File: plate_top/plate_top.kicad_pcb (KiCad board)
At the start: 2 copper layers, 157.5 x 118.1 mm, 31 parts, among them SW1 SW_Push

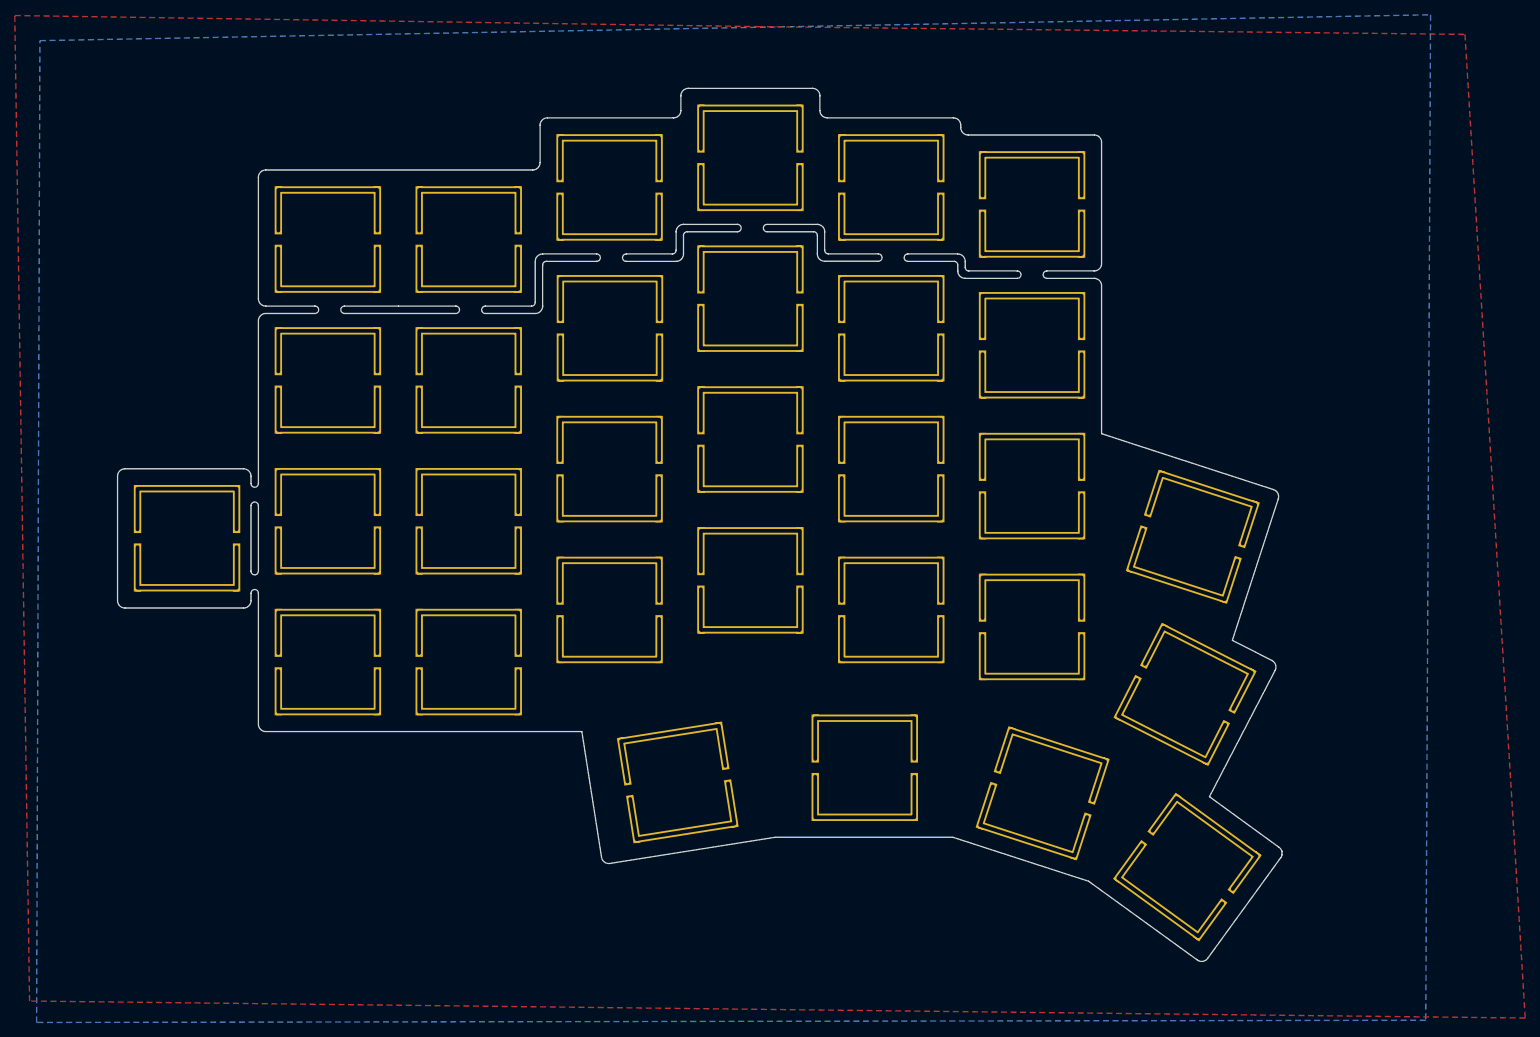
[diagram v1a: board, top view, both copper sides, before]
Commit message: Working on a new design for the top plate.
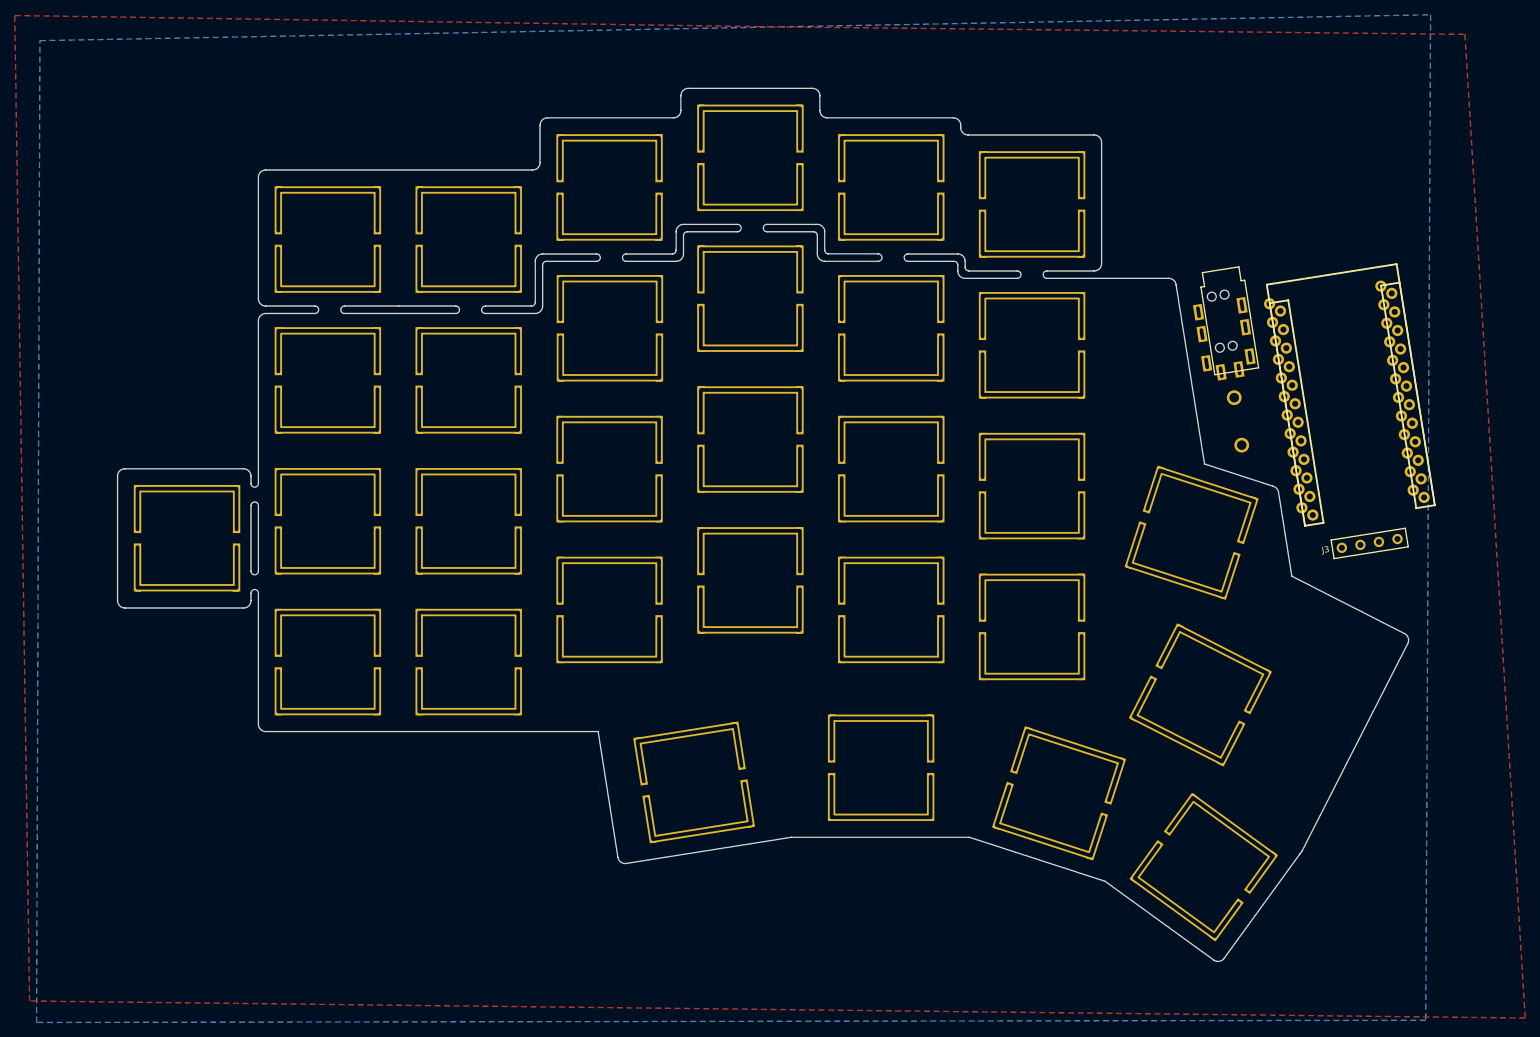
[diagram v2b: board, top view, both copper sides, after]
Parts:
- removed the SW1 at (221.3, 135.9)
- removed the SW1 at (201.7, 125.9)
- removed the SW1 at (177.6, 122.5)
- removed the SW1 at (152.3, 124.4)
- removed the SW1 at (220.9, 112.5)
- removed the SW1 at (222.0, 91.2)
- added J1: TRRS, used_footprints:MJ-4PP-9, F.Cu at (226.1, 57.0)
- added J3: OLED, used_footprints:OLED_4Pin, F.Cu at (242.2, 92.7)
- added SW20: SW_Push, used_footprints:metallized_breakout_cutout, F.Cu at (221.8, 90.7)
- added SW27: SW_Push, used_footprints:metallized_breakout_cutout, F.Cu at (223.0, 112.6)
- added SW28: SW_Push, used_footprints:metallized_breakout_cutout, F.Cu at (154.5, 124.4)
- added SW29: SW_Push, used_footprints:metallized_breakout_cutout, F.Cu at (179.8, 122.5)
- added SW30: SW_Push, used_footprints:metallized_breakout_cutout, F.Cu at (203.9, 125.9)
- added SW31: SW_Push, used_footprints:metallized_breakout_cutout, F.Cu at (223.5, 135.9)
- added SW32: SW_Push, used_footprints:Switch_Reset_THT, F.Cu at (228.1, 75.6)
- added U1: ProMicro, used_footprints:ProMicro_rev2, F.Cu at (243.4, 72.9)
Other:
- board size 157.5 x 118.1 mm -> 174.6 x 118.1 mm

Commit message: Multiple fixes...
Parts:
- moved SW32 32.4 mm to (251.4, 98.1), turned to 81 degrees

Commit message: top + bottom plates
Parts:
- removed J1: TRRS, used_footprints:MJ-4PP-9
- removed J3: OLED, used_footprints:OLED_4Pin
- removed the SW1 at (105.0, 89.1)
- removed the SW1 at (162.2, 40.0)
- removed the SW1 at (162.2, 59.0)
- removed the SW1 at (162.2, 78.0)
- removed the SW1 at (162.2, 97.1)
- removed the SW1 at (143.1, 101.1)
- removed the SW1 at (143.1, 82.0)
- removed the SW1 at (143.2, 63.0)
- removed the SW1 at (143.1, 44.0)
- removed the SW1 at (124.0, 51.0)
- removed the SW1 at (124.0, 70.0)
- removed the SW1 at (200.2, 103.4)
- removed the SW1 at (124.0, 89.1)
- removed the SW1 at (124.0, 108.2)
- removed the SW1 at (105.0, 108.2)
- removed the SW1 at (86.0, 91.4)
- removed the SW1 at (105.0, 70.0)
- removed the SW1 at (105.0, 51.0)
- removed the SW1 at (200.2, 84.3)
- removed the SW1 at (200.2, 65.3)
- removed the SW1 at (200.2, 46.2)
- removed the SW1 at (181.2, 101.1)
- removed the SW1 at (181.2, 82.0)
- removed the SW1 at (181.2, 63.0)
- removed the SW1 at (181.2, 44.0)
- removed U1: ProMicro, used_footprints:ProMicro_rev2
- added SW1: SW_Push, used_footprints:metallized_breakout_cutout, F.Cu at (100.2, 51.1)
- added SW10: SW_Push, used_footprints:metallized_breakout_cutout, F.Cu at (162.2, 59.0)
- added SW11: SW_Push, used_footprints:metallized_breakout_cutout, F.Cu at (181.2, 63.0)
- added SW12: SW_Push, used_footprints:metallized_breakout_cutout, F.Cu at (200.2, 65.3)
- added SW13: SW_Push, used_footprints:metallized_breakout_cutout, F.Cu at (103.2, 89.1)
- added SW14: SW_Push, used_footprints:metallized_breakout_cutout, F.Cu at (122.2, 87.6)
- added SW15: SW_Push, used_footprints:metallized_breakout_cutout, F.Cu at (143.1, 82.0)
- added SW16: SW_Push, used_footprints:metallized_breakout_cutout, F.Cu at (162.2, 78.0)
- added SW17: SW_Push, used_footprints:metallized_breakout_cutout, F.Cu at (181.2, 82.0)
- added SW18: SW_Push, used_footprints:metallized_breakout_cutout, F.Cu at (200.2, 84.3)
- added SW19: SW_Push, used_footprints:metallized_breakout_cutout, F.Cu at (220.7, 86.0)
- added SW2: SW_Push, used_footprints:metallized_breakout_cutout, F.Cu at (119.2, 49.6)
- added SW21: SW_Push, used_footprints:metallized_breakout_cutout, F.Cu at (123.7, 106.6)
- added SW22: SW_Push, used_footprints:metallized_breakout_cutout, F.Cu at (143.1, 101.1)
- added SW23: SW_Push, used_footprints:metallized_breakout_cutout, F.Cu at (162.2, 97.1)
- added SW24: SW_Push, used_footprints:metallized_breakout_cutout, F.Cu at (181.2, 101.1)
- added SW25: SW_Push, used_footprints:metallized_breakout_cutout, F.Cu at (200.2, 103.4)
- added SW26: SW_Push, used_footprints:metallized_breakout_cutout, F.Cu at (221.5, 108.3)
- added SW3: SW_Push, used_footprints:metallized_breakout_cutout, F.Cu at (143.1, 44.0)
- added SW4: SW_Push, used_footprints:metallized_breakout_cutout, F.Cu at (162.2, 40.0)
- added SW5: SW_Push, used_footprints:metallized_breakout_cutout, F.Cu at (181.2, 44.0)
- added SW6: SW_Push, used_footprints:metallized_breakout_cutout, F.Cu at (200.2, 46.2)
- added SW7: SW_Push, used_footprints:metallized_breakout_cutout, F.Cu at (101.7, 70.1)
- added SW8: SW_Push, used_footprints:metallized_breakout_cutout, F.Cu at (120.7, 68.6)
- added SW9: SW_Push, used_footprints:metallized_breakout_cutout, F.Cu at (143.1, 63.0)
- SW32: footprint used_footprints:Switch_Reset_THT -> used_footprints:metallized_breakout_cutout
- moved SW27 140.0 mm to (84.4, 92.9), turned to 184.5 degrees
- moved SW20 118.4 mm to (104.7, 108.1), turned to 184.5 degrees
- moved SW32 44.9 mm to (227.0, 135.8), turned to 324 degrees
- moved SW31 18.8 mm to (207.5, 125.9), turned to 342 degrees
- moved SW30 18.3 mm to (186.0, 122.5), turned to 0 degrees
- moved SW29 14.4 mm to (165.5, 124.1), turned to 9 degrees
- moved SW28 8.24 mm to (146.7, 127.0)
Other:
- board size 174.6 x 118.1 mm -> 177.4 x 117.9 mm

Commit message: Minor changes
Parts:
- added J1: TRRS, used_footprints:MJ-4PP-9, F.Cu at (226.1, 57.0)
- added SW0: SW_Push, used_footprints:Switch_Reset_THT, F.Cu at (251.4, 98.1)
- added U1: ProMicro, used_footprints:ProMicro_rev2, F.Cu at (243.4, 72.9)

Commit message: Generated gerbers for the Avalanche 2.0
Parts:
- removed J1: TRRS, used_footprints:MJ-4PP-9
- removed SW0: SW_Push, used_footprints:Switch_Reset_THT
- removed U1: ProMicro, used_footprints:ProMicro_rev2

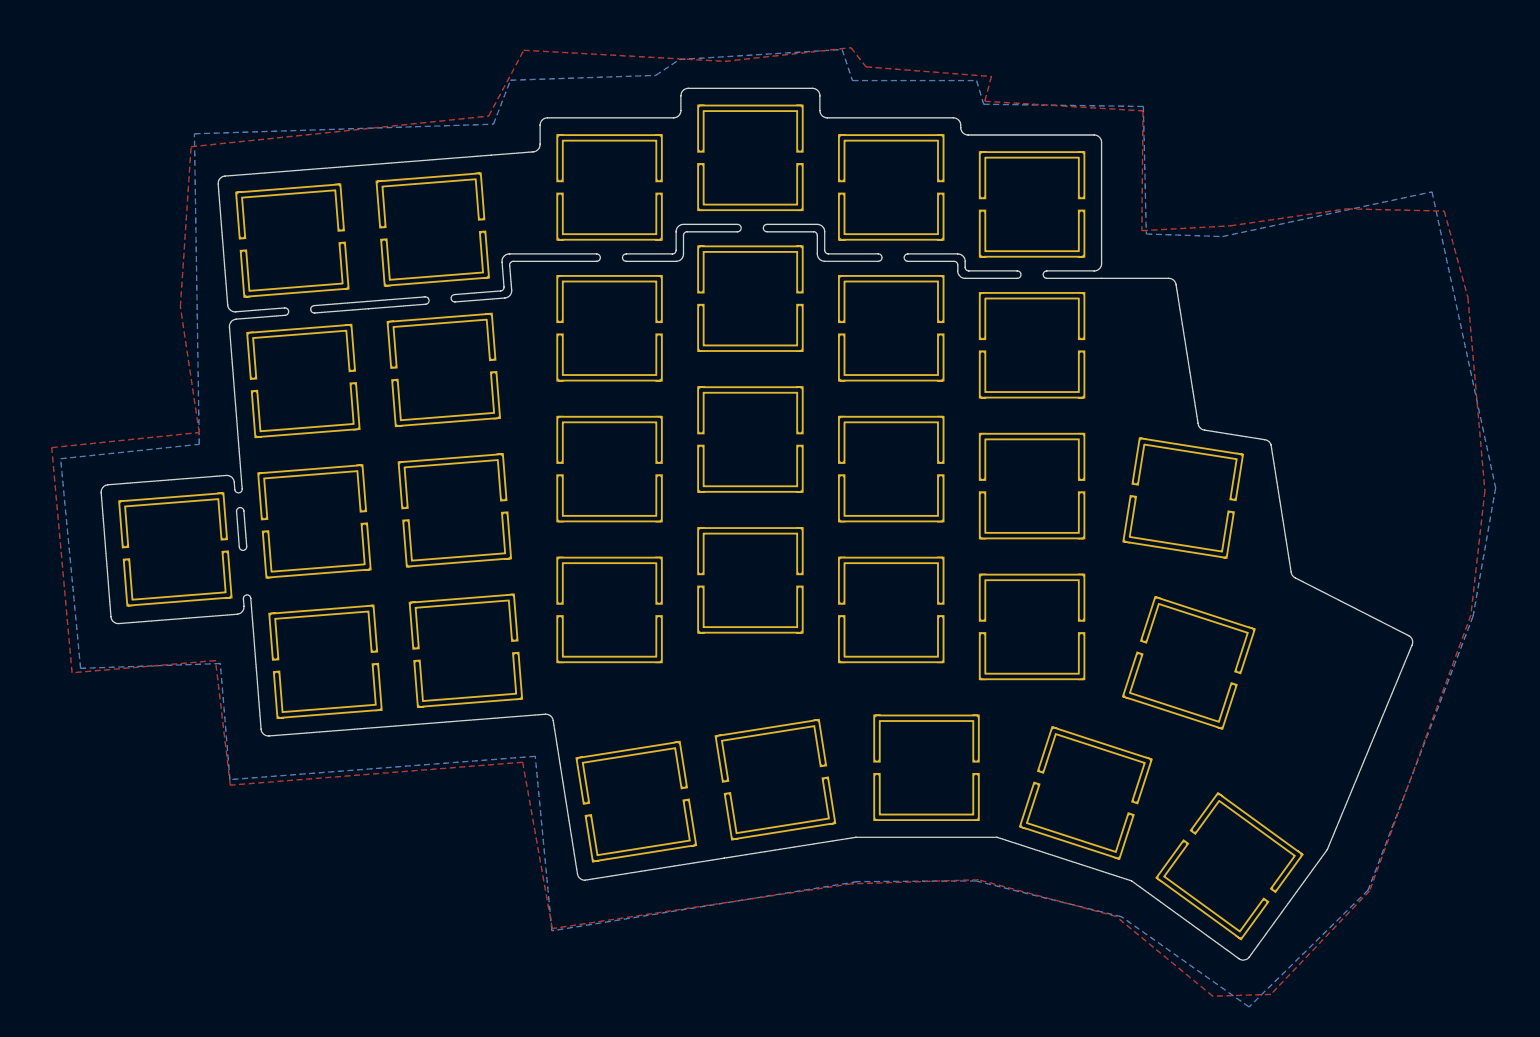
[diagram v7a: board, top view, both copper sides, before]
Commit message: Removed copper layers from top and bottom plates
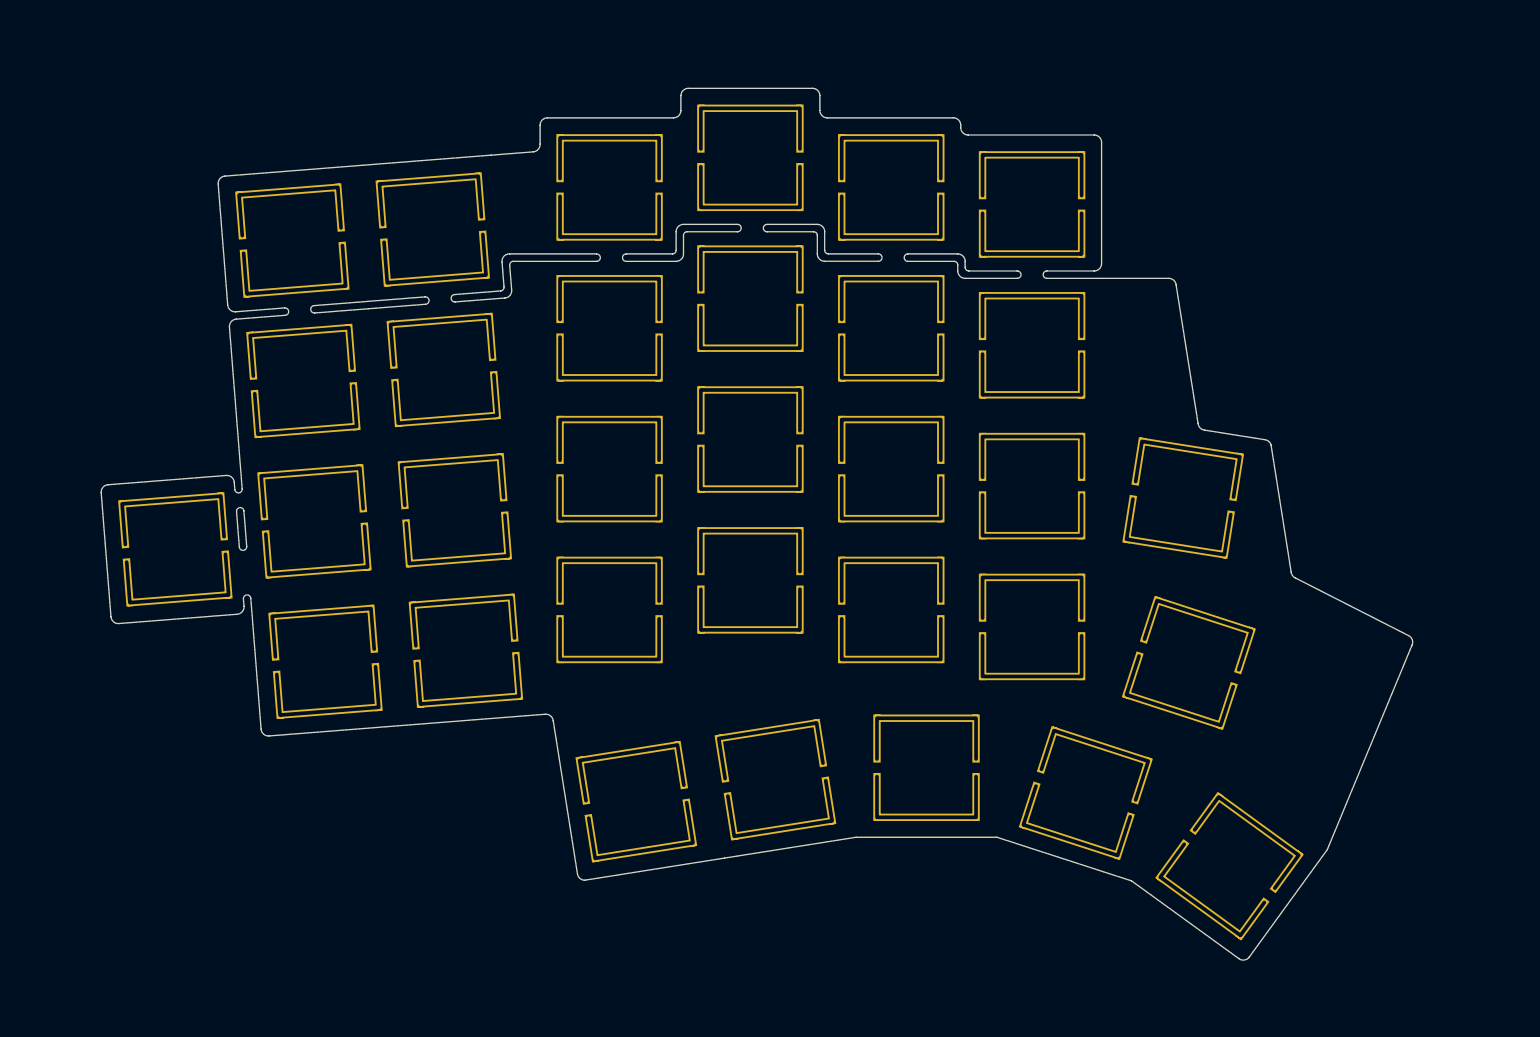
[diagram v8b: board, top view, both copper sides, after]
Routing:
- removed copper zone on B.Cu, net (none)
- removed copper zone on F.Cu, net (none)
